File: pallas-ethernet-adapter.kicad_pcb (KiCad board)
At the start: 4 copper layers, 69.3 x 51.8 mm, 88 parts, among them J1 PCIexpress_bracket, J2 PCIexpress_x1, J3 PPS, J4 IE-CLK, J5 RJ45_LED_Shielded, J6 RESET, J7 JTAG, U1 LAN7430, U2 93AAxxA, U3 SRV05-4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

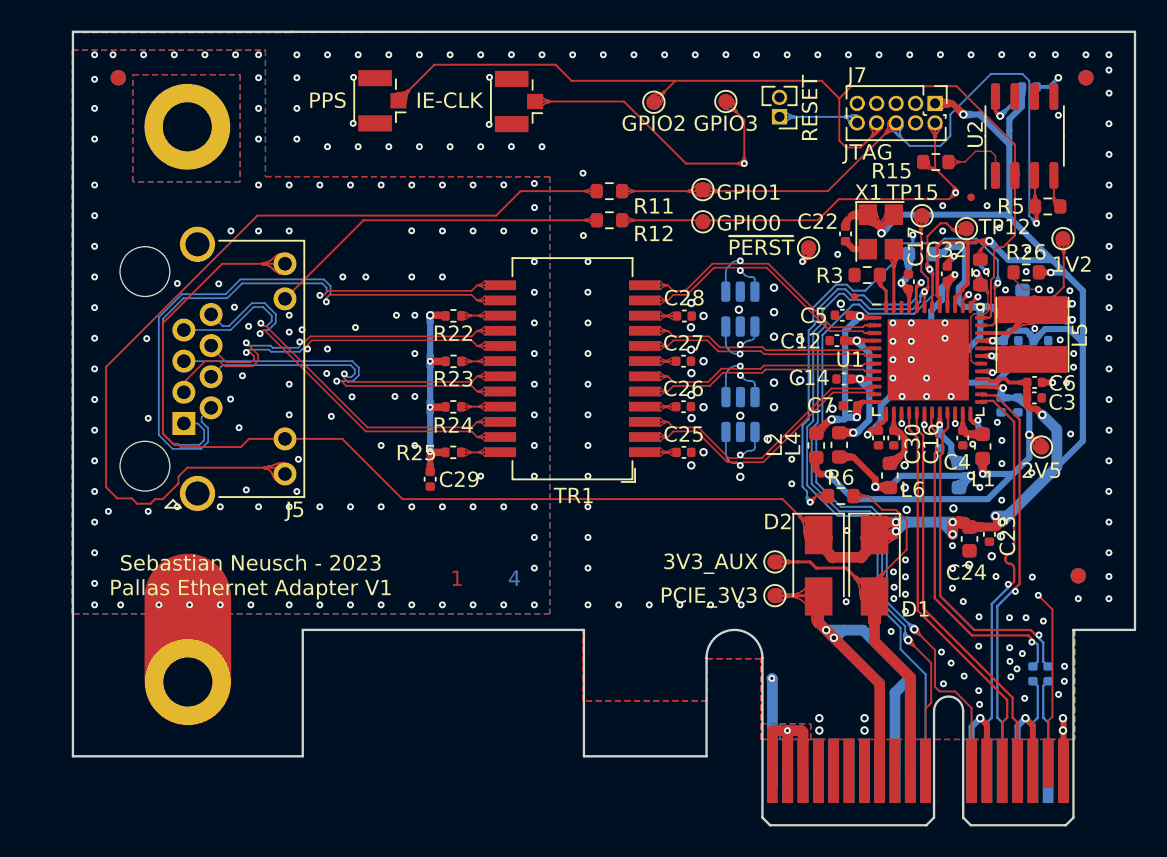
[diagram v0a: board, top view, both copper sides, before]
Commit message: * ground plane change to keep out beneath the magnetic module * changed RJ45 modular jack from tab up to tab down to improve the routing * added an 3d modell in the library folder for the rj45 connector * added a fitting footprint for SS74800-038F * changed width of the MDI and MII tracks to the JLC3313 stackup * changed impedance of the pcie lane from 100 Ohm differential to 85 Ohm and from 50 single ended to 45 ohm * impedace calculation pictures still missing
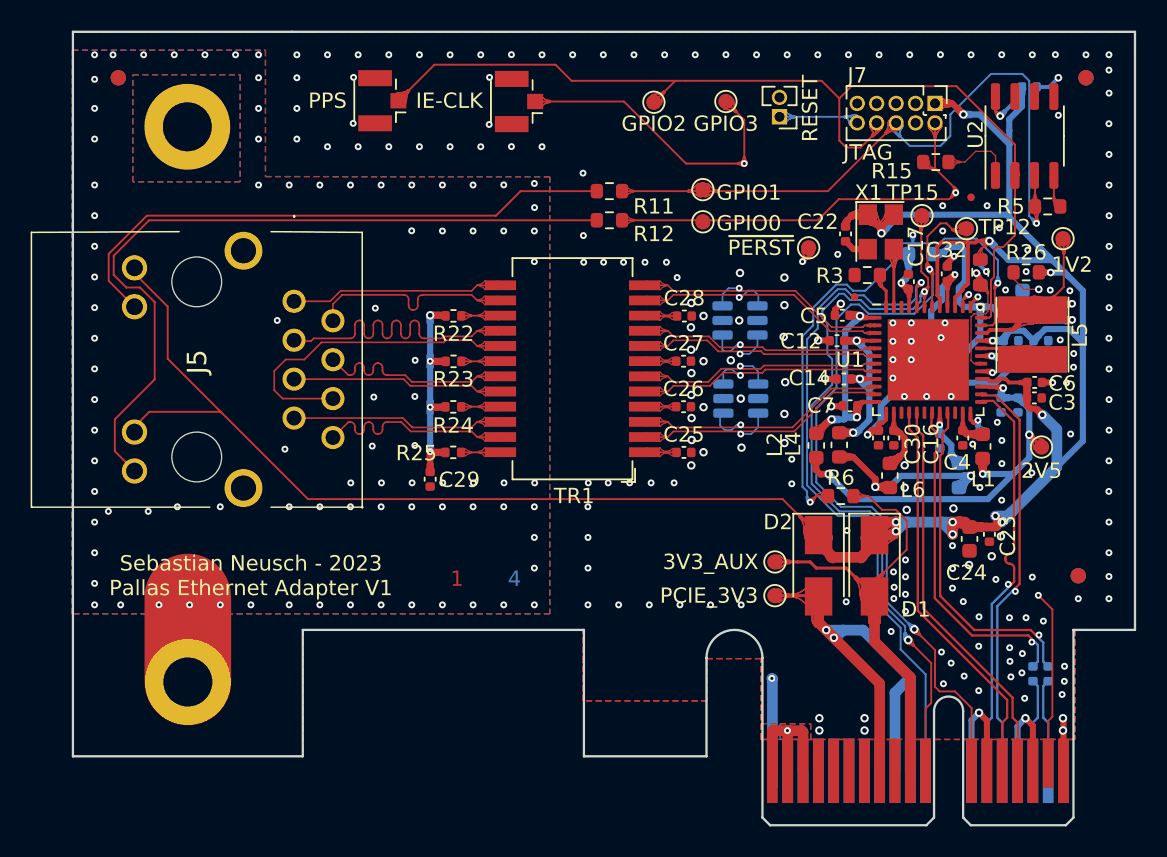
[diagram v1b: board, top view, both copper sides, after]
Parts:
- J5: footprint Connector_RJ:RJ45_Amphenol_RJHSE538X -> Library:SS74800038F
- moved J5 10.7 mm to (78.9, 159.9), turned to -90 degrees
- moved U3 1.04 mm to (108.1, 166.3), turned to 180 degrees
- moved U4 0.74 mm to (108.0, 161.2), turned to 180 degrees
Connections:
- U3 pad 1: /Ethernet/TXRX_D_P -> /Ethernet/TXRX_C_P
- U3 pad 4: /Ethernet/TXRX_C_P -> /Ethernet/TXRX_D_P
- U4 pad 1: /Ethernet/TXRX_B_P -> /Ethernet/TXRX_A_N
- U4 pad 4: /Ethernet/TXRX_A_P -> /Ethernet/TXRX_B_P
- U4 pad 6: /Ethernet/TXRX_A_N -> /Ethernet/TXRX_A_P
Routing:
- net /~{LED0}: track 22.5 -> 49.8 mm
- net /Ethernet/MDI_A_N: track 39.5 -> 13.9 mm, vias 1 -> 0
- net /Ethernet/MDI_A_P: track 37.4 -> 13.9 mm, vias 1 -> 0
- net /~{LED1}: track 58.2 -> 37.7 mm
- net /Ethernet/MDI_D_P: track 26.5 -> 13.9 mm, vias 1 -> 0
- net /Ethernet/MDI_D_N: track 26.0 -> 13.8 mm, vias 1 -> 0
- net /Ethernet/MDI_C_N: track 24.7 -> 13.8 mm, vias 1 -> 0
- net /Ethernet/MDI_C_P: track 21.7 -> 13.7 mm, vias 1 -> 0
- net /Ethernet/MDI_B_P: track 25.2 -> 20.9 mm, vias 2 -> 0
- net +3V3: track 178.0 -> 175.1 mm
- net /Ethernet/TXRX_D_N: track 21.1 -> 18.7 mm
- net /Ethernet/TXRX_A_P: track 20.5 -> 18.4 mm
- net GND: track 26.1 -> 27.8 mm
- net /Ethernet/TXRX_D_P: track 20.6 -> 19.0 mm
- net /LAN7430/VDD12_SW_OUT: track 3.67 -> 4.75 mm
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
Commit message: * moved magnetics to RJ45 connector for better EMI performance (still not enough though) * changed keepout layer beneath magnetics * moved meanders from magnetic side to connector side (from matched side to mismatched side)
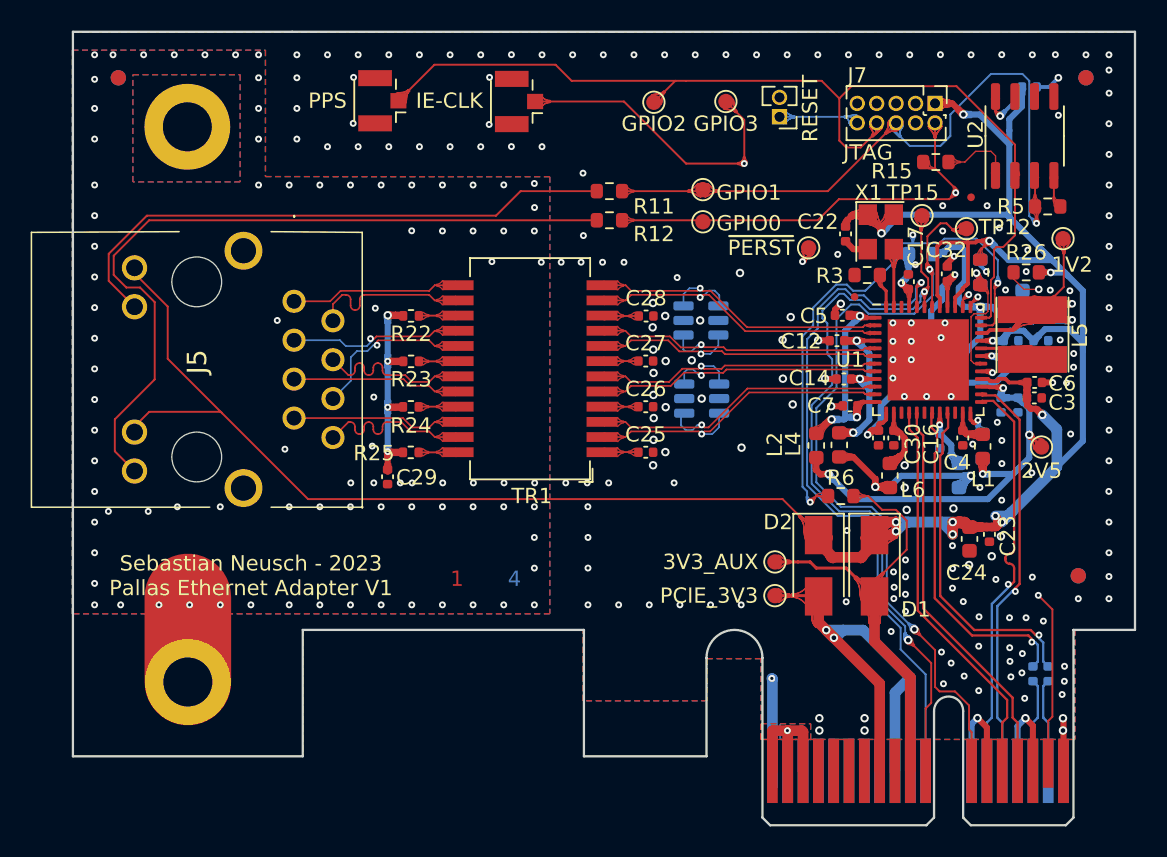
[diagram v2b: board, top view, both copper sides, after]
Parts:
- moved C29 2.78 mm to (85.0, 171.4)
- moved R23 2.77 mm to (86.5, 163.8)
- moved R22 2.77 mm to (86.5, 160.9)
- moved R24 2.77 mm to (86.5, 166.8)
- moved R25 2.77 mm to (86.5, 169.8)
- moved TR1 2.77 mm to (94.3, 164.3)
- moved U4 2.55 mm to (105.5, 161.2)
- moved U3 2.55 mm to (105.5, 166.3)
- moved C28 2.50 mm to (101.9, 160.9)
- moved C25 2.49 mm to (101.9, 169.8)
- moved C27 2.47 mm to (101.9, 163.8)
- moved C26 2.47 mm to (101.9, 166.8)
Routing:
- net /Ethernet/MDI_B_N: track 21.1 -> 10.9 mm, vias 0 -> 1
- net /Ethernet/MDI_B_P: track 20.9 -> 11.5 mm, vias 0 -> 1
- net /Ethernet/TXRX_C_P: track 18.0 -> 20.8 mm
- net /Ethernet/MDI_D_N: track 13.8 -> 11.0 mm
- net /Ethernet/MDI_C_N: track 13.8 -> 11.0 mm
- net /Ethernet/MDI_A_N: track 13.9 -> 11.1 mm
- net /Ethernet/TXRX_A_P: track 18.4 -> 21.2 mm
- net /Ethernet/TXRX_A_N: track 18.7 -> 21.5 mm
- net /Ethernet/MDI_D_P: track 13.9 -> 11.1 mm
- net /Ethernet/MDI_C_P: track 13.7 -> 10.9 mm
- net /Ethernet/MDI_A_P: track 13.9 -> 11.1 mm
- net /Ethernet/TXRX_B_N: track 17.9 -> 20.6 mm
- net /Ethernet/TXRX_B_P: track 18.1 -> 20.9 mm
- net /Ethernet/TXRX_C_N: track 18.0 -> 20.8 mm
- net /Ethernet/TXRX_D_P: track 19.0 -> 21.7 mm
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
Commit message: * corrected some drc errors like hole clearance, unconnected tracks etc.. * added screenshots of the impedance calculation in regards of the JLCPCB 3313 stackup * added picture of rendered 3d perspective * removed production directory (those were old production file)
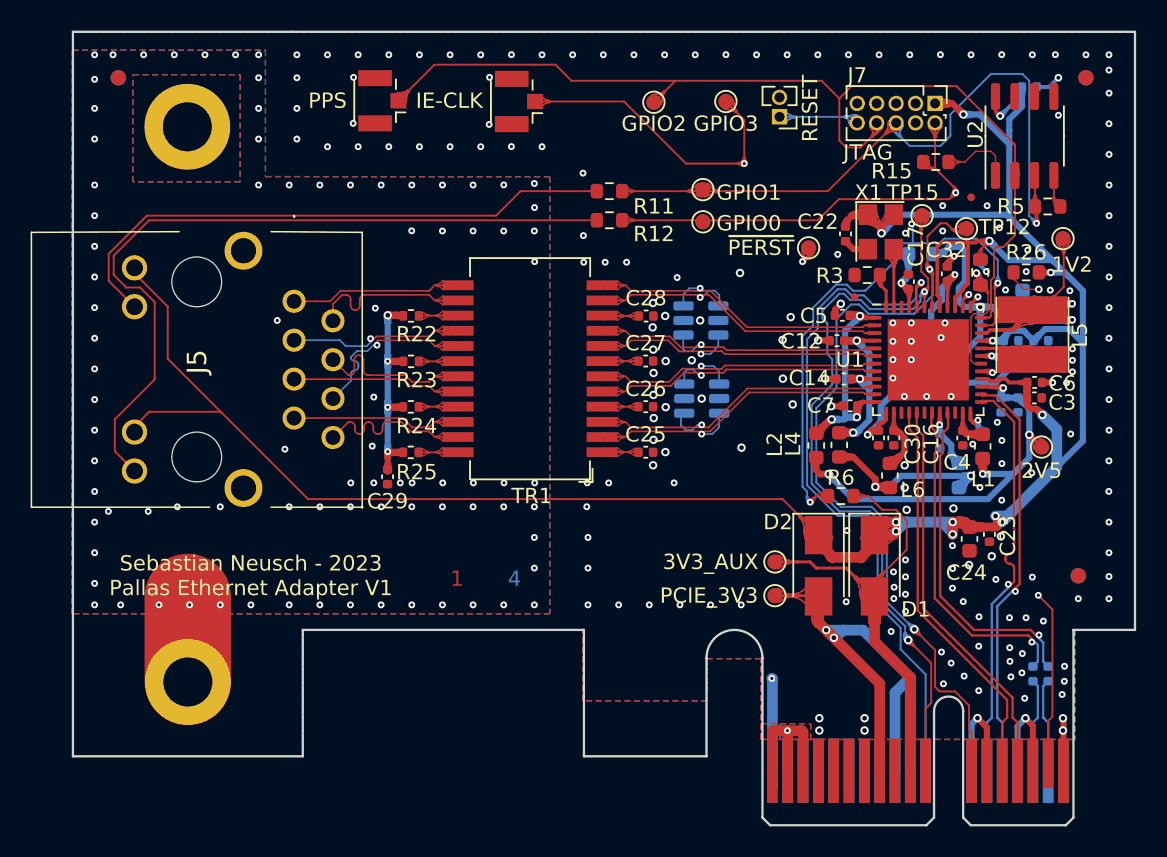
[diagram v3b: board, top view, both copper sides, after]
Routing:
- net /LAN_JTAG_TCK: track 76.1 -> 76.7 mm
- net /Ethernet/MDI_B_N: track 10.9 -> 11.5 mm
- net GND: vias 200 -> 196
- net /CASE: vias 86 -> 87
